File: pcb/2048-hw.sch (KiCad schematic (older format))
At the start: 98 parts, among them J1 UJC-HP-3-SMT-TR, J2 Battery, J3 SWD, SW1 SW_SPDT, SW2 PUSH_A, SW3 PUSH_B, U1 STM32F303K8Tx, U2 MCP73831-2-OT, U3 AP2210N-3.3TRG1, U4 PSP_1000_JSTK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

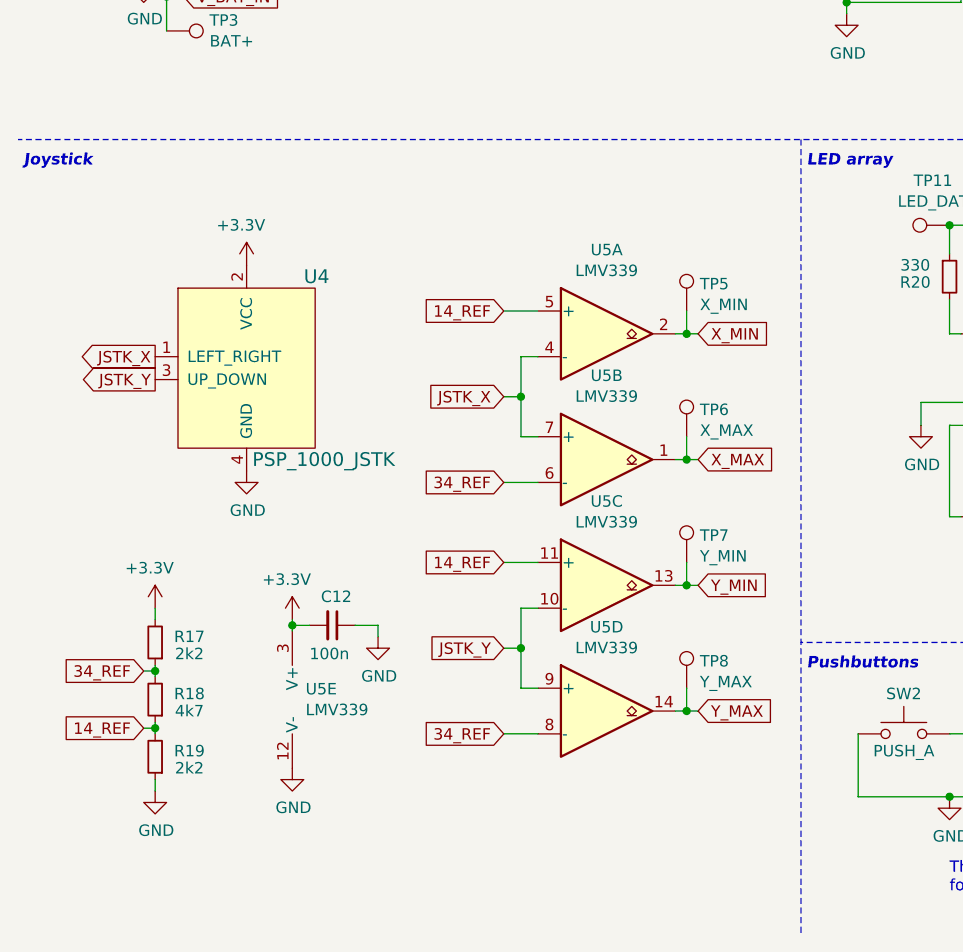
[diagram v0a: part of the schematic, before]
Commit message: Add mounting holes
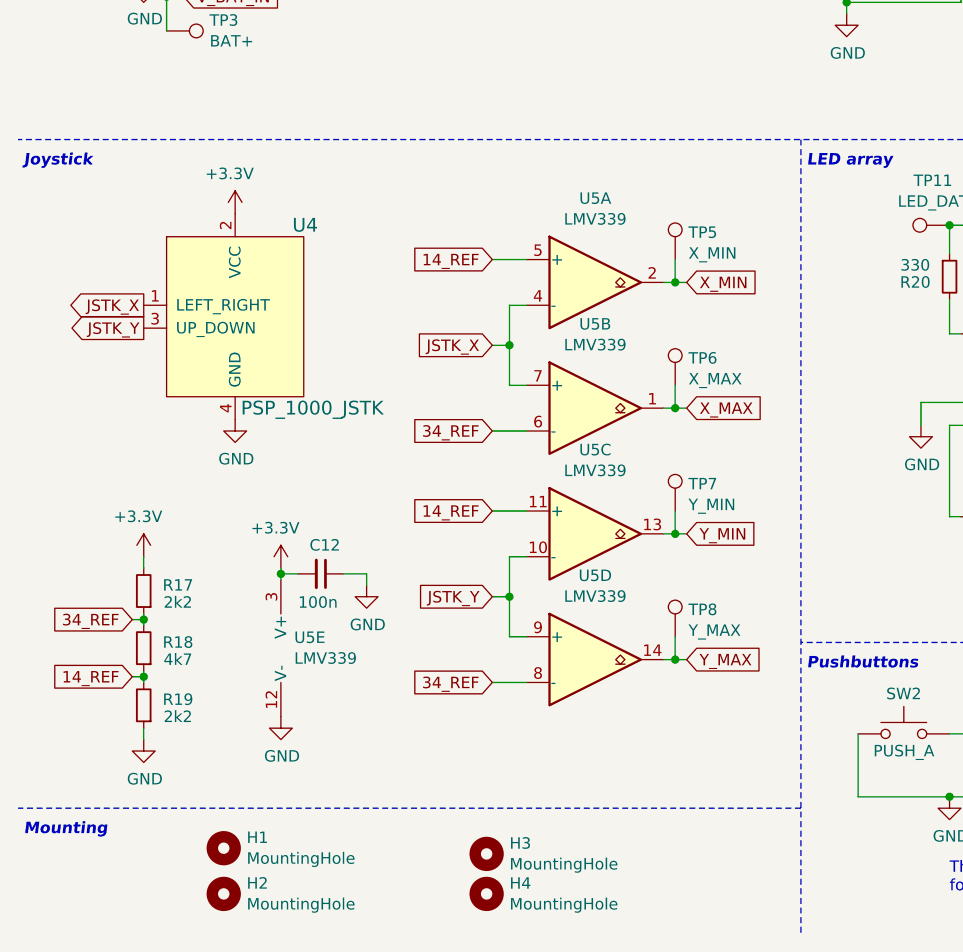
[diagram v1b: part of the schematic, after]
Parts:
- added H1, H2, H3, H4: MountingHole, MountingHole:MountingHole_2.2mm_M2, symbol Mechanical:MountingHole
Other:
- note added: "Mounting"
- moved on the sheet: C12, R17, R18, R19, TP5, TP6, TP7, TP8, U4, U5A, U5B, U5C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

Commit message: Use shorter power switch
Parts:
- SW1: footprint 2048-hw:E_SWITCH_EG2208A -> 2048-hw:E_SWITCH_EG2208
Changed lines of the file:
@@
 F 0 "SW1" H 1400 3685 50  0000 C CNN
 F 1 "SW_SPDT" H 1400 3594 50  0000 C CNN
-F 2 "2048-hw:E_SWITCH_EG2208A" H 1400 3400 50  0001 C CNN
+F 2 "2048-hw:E_SWITCH_EG2208" H 1400 3400 50  0001 C CNN
 F 3 "~" H 1400 3400 50  0001 C CNN
 	1    1400 3400

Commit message: Tidy up silkscreen and traces
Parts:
- D10, D11, D12, D13, D14, D15, D16, D17, D18, D19, D20, D21, D6, D7, D8, D9: footprint LED_SMD:LED_WS2812B_PLCC4_5.0x5.0mm_P3.2mm -> 2048-hw:LED_WS2812B_PLCC4_5.0x5.0mm_P3.2mm_no1
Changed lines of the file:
@@
 Title "2048-hw"
 Date "2021-01-02"
-Rev "0.1"
+Rev "1.0"
 Comp ""
 Comment1 "Original game is located at https://play2048.co/"
@@
 F 0 "D8" H 6475 5425 50  0000 L CNN
 F 1 "WS2812B" H 6450 4925 50  0000 L CNN
-F 2 "LED_SMD:LED_WS2812B_PLCC4_5.0x5.0mm_P3.2mm" H 6400 4875 50  0001 L TNN
+F 2 "2048-hw:LED_WS2812B_PLCC4_5.0x5.0mm_P3.2mm_no1" H 6400 4875 50  0001 L TNN
 F 3 "https://cdn-shop.adafruit.com/datasheets/WS2812B.pdf" H 6450 4800 50  0001 L TNN
 	1    6350 5175
@@
 F 0 "D7" H 5750 5425 50  0000 L CNN
 F 1 "WS2812B" H 5725 4925 50  0000 L CNN
-F 2 "LED_SMD:LED_WS2812B_PLCC4_5.0x5.0mm_P3.2mm" H 5675 4875 50  0001 L TNN
+F 2 "2048-hw:LED_WS2812B_PLCC4_5.0x5.0mm_P3.2mm_no1" H 5675 4875 50  0001 L TNN
 F 3 "https://cdn-shop.adafruit.com/datasheets/WS2812B.pdf" H 5725 4800 50  0001 L TNN
 	1    5625 5175
@@
 F 0 "D6" H 5025 5425 50  0000 L CNN
 F 1 "WS2812B" H 5000 4925 50  0000 L CNN
-F 2 "LED_SMD:LED_WS2812B_PLCC4_5.0x5.0mm_P3.2mm" H 4950 4875 50  0001 L TNN
+F 2 "2048-hw:LED_WS2812B_PLCC4_5.0x5.0mm_P3.2mm_no1" H 4950 4875 50  0001 L TNN
 F 3 "https://cdn-shop.adafruit.com/datasheets/WS2812B.pdf" H 5000 4800 50  0001 L TNN
 	1    4900 5175
@@
 F 0 "D9" H 7200 5425 50  0000 L CNN
 F 1 "WS2812B" H 7175 4925 50  0000 L CNN
-F 2 "LED_SMD:LED_WS2812B_PLCC4_5.0x5.0mm_P3.2mm" H 7125 4875 50  0001 L TNN
+F 2 "2048-hw:LED_WS2812B_PLCC4_5.0x5.0mm_P3.2mm_no1" H 7125 4875 50  0001 L TNN
 F 3 "https://cdn-shop.adafruit.com/datasheets/WS2812B.pdf" H 7175 4800 50  0001 L TNN
 	1    7075 5175
@@
 F 0 "D10" H 7925 5425 50  0000 L CNN
 F 1 "WS2812B" H 7900 4925 50  0000 L CNN
-F 2 "LED_SMD:LED_WS2812B_PLCC4_5.0x5.0mm_P3.2mm" H 7850 4875 50  0001 L TNN
+F 2 "2048-hw:LED_WS2812B_PLCC4_5.0x5.0mm_P3.2mm_no1" H 7850 4875 50  0001 L TNN
 F 3 "https://cdn-shop.adafruit.com/datasheets/WS2812B.pdf" H 7900 4800 50  0001 L TNN
 	1    7800 5175
@@
 F 0 "D11" H 8650 5425 50  0000 L CNN
 F 1 "WS2812B" H 8625 4925 50  0000 L CNN
-F 2 "LED_SMD:LED_WS2812B_PLCC4_5.0x5.0mm_P3.2mm" H 8575 4875 50  0001 L TNN
+F 2 "2048-hw:LED_WS2812B_PLCC4_5.0x5.0mm_P3.2mm_no1" H 8575 4875 50  0001 L TNN
 F 3 "https://cdn-shop.adafruit.com/datasheets/WS2812B.pdf" H 8625 4800 50  0001 L TNN
 	1    8525 5175
@@
 F 0 "D13" H 10100 5425 50  0000 L CNN
 F 1 "WS2812B" H 10075 4925 50  0000 L CNN
-F 2 "LED_SMD:LED_WS2812B_PLCC4_5.0x5.0mm_P3.2mm" H 10025 4875 50  0001 L TNN
+F 2 "2048-hw:LED_WS2812B_PLCC4_5.0x5.0mm_P3.2mm_no1" H 10025 4875 50  0001 L TNN
 F 3 "https://cdn-shop.adafruit.com/datasheets/WS2812B.pdf" H 10075 4800 50  0001 L TNN
 	1    9975 5175
@@
 F 0 "D12" H 9375 5425 50  0000 L CNN
 F 1 "WS2812B" H 9350 4925 50  0000 L CNN
-F 2 "LED_SMD:LED_WS2812B_PLCC4_5.0x5.0mm_P3.2mm" H 9300 4875 50  0001 L TNN
+F 2 "2048-hw:LED_WS2812B_PLCC4_5.0x5.0mm_P3.2mm_no1" H 9300 4875 50  0001 L TNN
 F 3 "https://cdn-shop.adafruit.com/datasheets/WS2812B.pdf" H 9350 4800 50  0001 L TNN
 	1    9250 5175
@@
 F 0 "D16" H 6475 6225 50  0000 L CNN
 F 1 "WS2812B" H 6450 5725 50  0000 L CNN
-F 2 "LED_SMD:LED_WS2812B_PLCC4_5.0x5.0mm_P3.2mm" H 6400 5675 50  0001 L TNN
+F 2 "2048-hw:LED_WS2812B_PLCC4_5.0x5.0mm_P3.2mm_no1" H 6400 5675 50  0001 L TNN
 F 3 "https://cdn-shop.adafruit.com/datasheets/WS2812B.pdf" H 6450 5600 50  0001 L TNN
 	1    6350 5975
@@
 F 0 "D15" H 5750 6225 50  0000 L CNN
 F 1 "WS2812B" H 5725 5725 50  0000 L CNN
-F 2 "LED_SMD:LED_WS2812B_PLCC4_5.0x5.0mm_P3.2mm" H 5675 5675 50  0001 L TNN
+F 2 "2048-hw:LED_WS2812B_PLCC4_5.0x5.0mm_P3.2mm_no1" H 5675 5675 50  0001 L TNN
 F 3 "https://cdn-shop.adafruit.com/datasheets/WS2812B.pdf" H 5725 5600 50  0001 L TNN
 	1    5625 5975
@@
 F 0 "D14" H 5025 6225 50  0000 L CNN
 F 1 "WS2812B" H 5000 5725 50  0000 L CNN
-F 2 "LED_SMD:LED_WS2812B_PLCC4_5.0x5.0mm_P3.2mm" H 4950 5675 50  0001 L TNN
+F 2 "2048-hw:LED_WS2812B_PLCC4_5.0x5.0mm_P3.2mm_no1" H 4950 5675 50  0001 L TNN
 F 3 "https://cdn-shop.adafruit.com/datasheets/WS2812B.pdf" H 5000 5600 50  0001 L TNN
 	1    4900 5975
@@
 F 0 "D17" H 7200 6225 50  0000 L CNN
 F 1 "WS2812B" H 7175 5725 50  0000 L CNN
-F 2 "LED_SMD:LED_WS2812B_PLCC4_5.0x5.0mm_P3.2mm" H 7125 5675 50  0001 L TNN
+F 2 "2048-hw:LED_WS2812B_PLCC4_5.0x5.0mm_P3.2mm_no1" H 7125 5675 50  0001 L TNN
 F 3 "https://cdn-shop.adafruit.com/datasheets/WS2812B.pdf" H 7175 5600 50  0001 L TNN
 	1    7075 5975
@@
 F 0 "D18" H 7925 6225 50  0000 L CNN
 F 1 "WS2812B" H 7900 5725 50  0000 L CNN
-F 2 "LED_SMD:LED_WS2812B_PLCC4_5.0x5.0mm_P3.2mm" H 7850 5675 50  0001 L TNN
+F 2 "2048-hw:LED_WS2812B_PLCC4_5.0x5.0mm_P3.2mm_no1" H 7850 5675 50  0001 L TNN
 F 3 "https://cdn-shop.adafruit.com/datasheets/WS2812B.pdf" H 7900 5600 50  0001 L TNN
 	1    7800 5975
@@
 F 0 "D19" H 8650 6225 50  0000 L CNN
 F 1 "WS2812B" H 8625 5725 50  0000 L CNN
-F 2 "LED_SMD:LED_WS2812B_PLCC4_5.0x5.0mm_P3.2mm" H 8575 5675 50  0001 L TNN
+F 2 "2048-hw:LED_WS2812B_PLCC4_5.0x5.0mm_P3.2mm_no1" H 8575 5675 50  0001 L TNN
 F 3 "https://cdn-shop.adafruit.com/datasheets/WS2812B.pdf" H 8625 5600 50  0001 L TNN
 	1    8525 5975
@@
 F 0 "D21" H 10100 6225 50  0000 L CNN
 F 1 "WS2812B" H 10075 5725 50  0000 L CNN
-F 2 "LED_SMD:LED_WS2812B_PLCC4_5.0x5.0mm_P3.2mm" H 10025 5675 50  0001 L TNN
+F 2 "2048-hw:LED_WS2812B_PLCC4_5.0x5.0mm_P3.2mm_no1" H 10025 5675 50  0001 L TNN
 F 3 "https://cdn-shop.adafruit.com/datasheets/WS2812B.pdf" H 10075 5600 50  0001 L TNN
 	1    9975 5975
@@
 F 0 "D20" H 9375 6225 50  0000 L CNN
 F 1 "WS2812B" H 9350 5725 50  0000 L CNN
-F 2 "LED_SMD:LED_WS2812B_PLCC4_5.0x5.0mm_P3.2mm" H 9300 5675 50  0001 L TNN
+F 2 "2048-hw:LED_WS2812B_PLCC4_5.0x5.0mm_P3.2mm_no1" H 9300 5675 50  0001 L TNN
 F 3 "https://cdn-shop.adafruit.com/datasheets/WS2812B.pdf" H 9350 5600 50  0001 L TNN
 	1    9250 5975

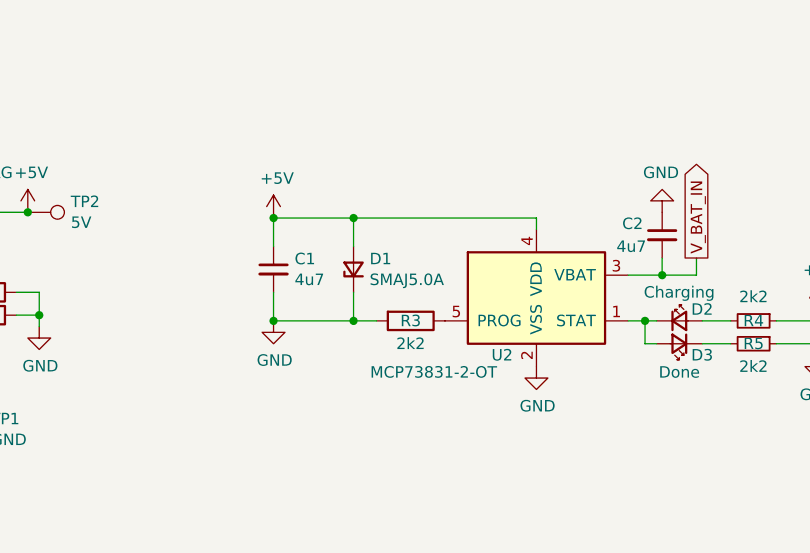
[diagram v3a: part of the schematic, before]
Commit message: Reverse the backwards zener diode
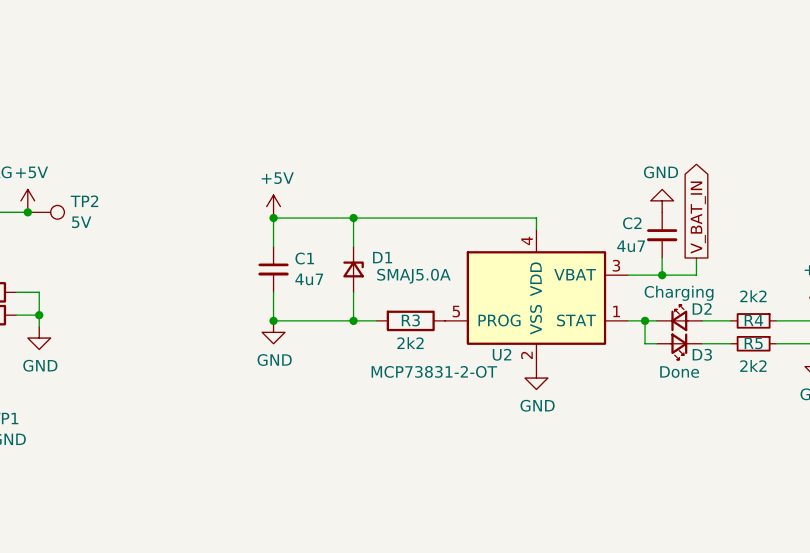
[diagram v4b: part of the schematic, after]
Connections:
- net +5V: now also D1.1 (K); no longer D1.2 (A)
- net GND: now also D1.2 (A); no longer D1.1 (K)
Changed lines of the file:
@@
-$EndComp
-$Comp
-L Device:D_Zener_Small D1
-U 1 1 5FF1E4E4
-P 3725 1575
-F 0 "D1" V 3771 1505 50  0000 R CNN
-F 1 "SMAJ5.0A" V 3680 1505 50  0000 R CNN
-F 2 "Diode_SMD:D_SMA_Handsoldering" V 3725 1575 50  0001 C CNN
-F 3 "~" V 3725 1575 50  0001 C CNN
-	1    3725 1575
-	0    -1   -1   0
 $EndComp
 $Comp
@@
 	1    0    0    -1
 $EndComp
+$Comp
+L Device:D_Zener_Small D1
+U 1 1 5FF1E4E4
+P 3725 1575
+F 0 "D1" V 3675 1750 50  0000 R CNN
+F 1 "SMAJ5.0A" V 3750 2000 50  0000 R CNN
+F 2 "Diode_SMD:D_SMA_Handsoldering" V 3725 1575 50  0001 C CNN
+F 3 "~" V 3725 1575 50  0001 C CNN
+	1    3725 1575
+	0    1    1    0
+$EndComp
 $EndSCHEMATC

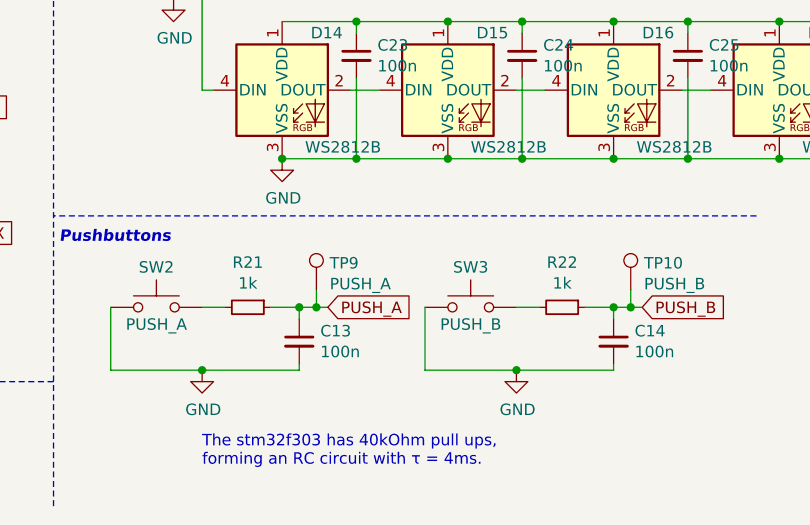
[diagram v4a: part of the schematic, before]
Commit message: Update component values for BOM
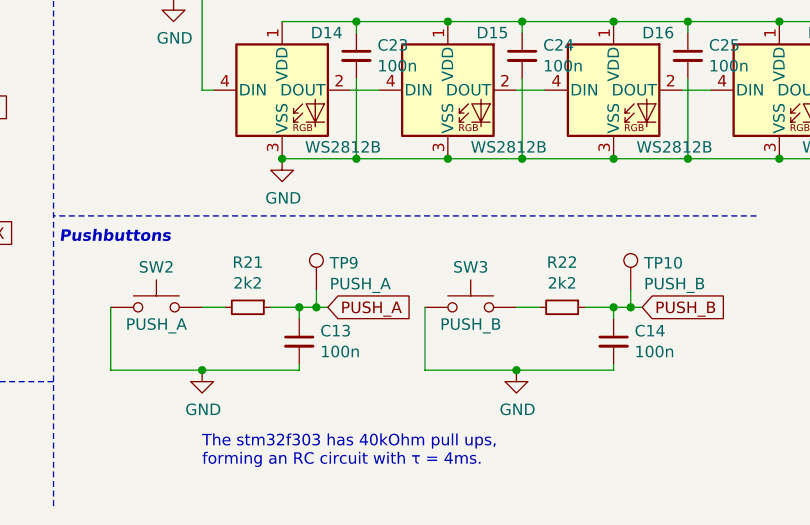
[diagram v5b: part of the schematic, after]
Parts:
- R21, R22: value 1k -> 2k2
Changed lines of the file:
@@
 P 4750 6925
 F 0 "R21" V 4554 6925 50  0000 C CNN
-F 1 "1k" V 4645 6925 50  0000 C CNN
+F 1 "2k2" V 4645 6925 50  0000 C CNN
 F 2 "Resistor_SMD:R_0603_1608Metric_Pad0.98x0.95mm_HandSolder" H 4750 6925 50  0001 C CNN
 F 3 "~" H 4750 6925 50  0001 C CNN
@@
 P 6125 6925
 F 0 "R22" V 5929 6925 50  0000 C CNN
-F 1 "1k" V 6020 6925 50  0000 C CNN
+F 1 "2k2" V 6020 6925 50  0000 C CNN
 F 2 "Resistor_SMD:R_0603_1608Metric_Pad0.98x0.95mm_HandSolder" H 6125 6925 50  0001 C CNN
 F 3 "~" H 6125 6925 50  0001 C CNN

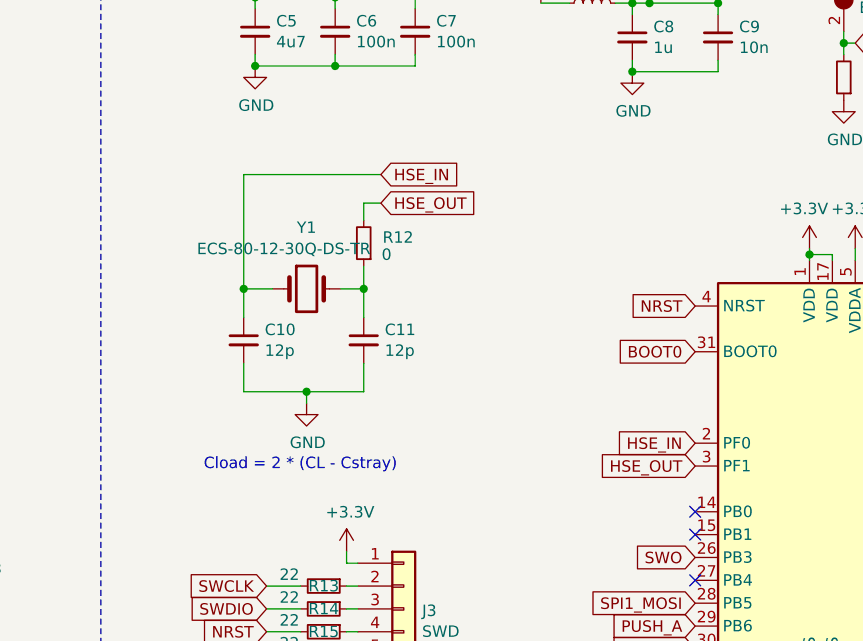
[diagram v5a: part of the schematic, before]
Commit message: pcb: Remove crystal
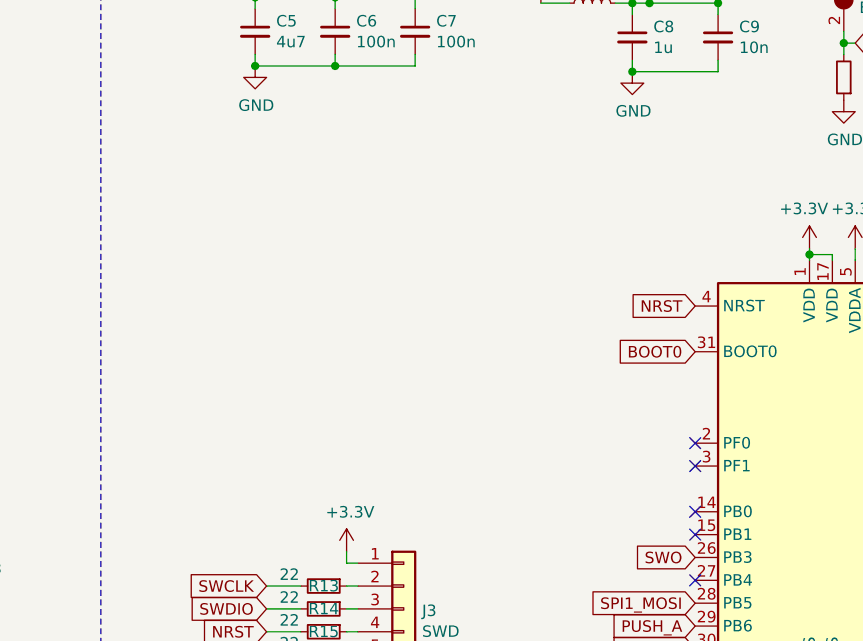
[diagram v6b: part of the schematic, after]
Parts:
- removed C10, C11: 12p, Capacitor_SMD:C_0603_1608Metric_Pad1.08x0.95mm_HandSolder, symbol Device:C_Small
- removed R12: 0, Resistor_SMD:R_0603_1608Metric_Pad0.98x0.95mm_HandSolder, symbol Device:R_Small
- removed Y1: ECS-80-12-30Q-DS-TR, 2048-hw:XTAL_ECS-80-18-30-JGN-TR, symbol Device:Crystal
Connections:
- net HSE_IN: no longer names the net of U1.2 (PF0)
- net HSE_OUT: no longer names the net of U1.3 (PF1)
- no-connect marks 13 -> 15
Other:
- note removed: "Cload = 2 * (CL - Cstray)"
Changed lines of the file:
@@
 Text GLabel 10325 3225 2    50   Input ~ 0
 X_MIN
-Text Notes 7075 3150 0    50   ~ 0
-Cload = 2 * (CL - Cstray)
-Wire Wire Line
-	7250 1850 7850 1850
-Connection ~ 7525 2800
-Wire Wire Line
-	7775 2800 7525 2800
-Connection ~ 7250 2350
-Wire Wire Line
-	7250 1850 7250 2350
-Wire Wire Line
-	7775 1975 7775 2050
-Wire Wire Line
-	7850 1975 7775 1975
-Text GLabel 7850 1975 2    50   Input ~ 0
-HSE_OUT
-Text GLabel 7850 1850 2    50   Input ~ 0
-HSE_IN
-Connection ~ 7775 2350
-Wire Wire Line
-	7775 2350 7775 2250
-$Comp
-L Device:R_Small R12
-U 1 1 5FFB6F1D
-P 7775 2150
-F 0 "R12" H 7625 2125 50  0000 C CNN
-F 1 "0" H 7675 2200 50  0000 C CNN
-F 2 "Resistor_SMD:R_0603_1608Metric_Pad0.98x0.95mm_HandSolder" H 7775 2150 50  0001 C CNN
-F 3 "~" H 7775 2150 50  0001 C CNN
-	1    7775 2150
-	-1   0    0    1
-$EndComp
-Wire Wire Line
-	7525 2850 7525 2800
-$Comp
-L power:GND #PWR012
-U 1 1 5FFB4828
-P 7525 2850
-F 0 "#PWR012" H 7525 2600 50  0001 C CNN
-F 1 "GND" H 7530 2677 50  0000 C CNN
-F 2 "" H 7525 2850 50  0001 C CNN
-F 3 "" H 7525 2850 50  0001 C CNN
-	1    7525 2850
-	1    0    0    -1
-$EndComp
-Wire Wire Line
-	7775 2800 7775 2675
-Wire Wire Line
-	7250 2800 7525 2800
-Wire Wire Line
-	7250 2675 7250 2800
-Wire Wire Line
-	7250 2350 7375 2350
-Wire Wire Line
-	7250 2475 7250 2350
-Wire Wire Line
-	7775 2350 7675 2350
-Wire Wire Line
-	7775 2475 7775 2350
-$Comp
-L Device:C_Small C11
-U 1 1 5FFAB48B
-P 7775 2575
-F 0 "C11" H 7867 2621 50  0000 L CNN
-F 1 "12p" H 7867 2530 50  0000 L CNN
-F 2 "Capacitor_SMD:C_0603_1608Metric_Pad1.08x0.95mm_HandSolder" H 7775 2575 50  0001 C CNN
-F 3 "~" H 7775 2575 50  0001 C CNN
-	1    7775 2575
-	1    0    0    -1
-$EndComp
-$Comp
-L Device:C_Small C10
-U 1 1 5FFAAB69
-P 7250 2575
-F 0 "C10" H 7342 2621 50  0000 L CNN
-F 1 "12p" H 7342 2530 50  0000 L CNN
-F 2 "Capacitor_SMD:C_0603_1608Metric_Pad1.08x0.95mm_HandSolder" H 7250 2575 50  0001 C CNN
-F 3 "~" H 7250 2575 50  0001 C CNN
-	1    7250 2575
-	1    0    0    -1
-$EndComp
 Wire Wire Line
 	8550 1100 8675 1100
@@
 Text GLabel 10325 3725 2    50   Input ~ 0
 SWDIO
-Text GLabel 9225 3125 0    50   Input ~ 0
-HSE_OUT
-Text GLabel 9225 3025 0    50   Input ~ 0
-HSE_IN
 Text GLabel 9225 2425 0    50   Input ~ 0
 NRST
@@
 	1    0    0    -1
 $EndComp
-$Comp
-L Device:Crystal Y1
-U 1 1 5FFA9BCF
-P 7525 2350
-F 0 "Y1" H 7525 2618 50  0000 C CNN
-F 1 " ECS-80-12-30Q-DS-TR" H 7425 2525 50  0000 C CNN
-F 2 "2048-hw:XTAL_ECS-80-18-30-JGN-TR" H 7525 2350 50  0001 C CNN
-F 3 "~" H 7525 2350 50  0001 C CNN
-	1    7525 2350
-	1    0    0    -1
-$EndComp
 Wire Wire Line
 	1400 2425 1300 2425
@@
 	0    1    1    0
 $EndComp
+NoConn ~ 9225 3025
+NoConn ~ 9225 3125
 $EndSCHEMATC
